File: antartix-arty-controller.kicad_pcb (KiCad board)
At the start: 2 copper layers, 68.5 x 40 mm, 77 parts, among them IC1 FT2232D, J1 QTE-020-04-L-D-A, J2 614004185023, J3 614004185023, J4 614004185023, J5 WE_629105150521, U1 PCT2075GVX, U2 PAC1934T-I_JQ, U3 USB2514B-I_M2, U4 TPS2051BDBVR, U5 TPS2051BDBVR, U6 TPS2051BDBVR, U7 TPS2051BDBVR, Y1 7C-24.000MBB-T, Y2 MQ-6.000-12-30_30_

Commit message: Layout update (WIP)
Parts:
- added C27: C_100n_0402, antartix-arty-controller-footprints:0402-cap, B.Cu at (160.1, 88.8)
- added D7: LG_L29K-G2J1-24-Z, antartix-arty-controller-footprints:LED_0603, F.Cu at (154.1, 61.0)
- added R28: R_0R_0805, antmicro-footprints:0805-res, B.Cu at (160.7, 84.8)
- added R29: R_0R_0805, antmicro-footprints:0805-res, B.Cu at (160.7, 87.2)
- added R30: R_47k_0402, antartix-arty-controller-footprints:0402-res, F.Cu at (152.8, 61.4)
- added R31: R_12k_0402, antmicro-footprints:0402-res, F.Cu at (153.5, 70.6)
- 3V0: renamed from 3V1; moved to F.Cu
- 5V0: renamed from 5V1; moved to F.Cu
- C10, C11, C12, C13, C14, C15, C16, C17, C18, C19, C20, C21, C23, C25, C9, D2, D3, D4, D5, FB1, R10, R11, R12, R13, R15, R16, R17, R19, R20, R21, R22, R25, R26, R27, U7: moved to F.Cu
- R23, R24, R4, R5, R6, R7, R8: moved to B.Cu
- moved R10 111.2 mm to (110.3, 80.3), turned to 0 degrees
- moved R12 109.5 mm to (110.3, 77.1), turned to 0 degrees
- moved R13 103.7 mm to (110.3, 75.4), turned to 0 degrees
- moved R11 98.9 mm to (110.3, 78.7)
- moved D5 88.8 mm to (113.1, 75.4), turned to 180 degrees
- moved D4 85.5 mm to (113.1, 77.1), turned to 180 degrees
- moved D3 85.5 mm to (113.1, 78.7), turned to 180 degrees
- moved D2 83.0 mm to (113.1, 80.3), turned to 180 degrees
- moved C26 76.5 mm to (136.9, 55.0), turned to 90 degrees
- moved 3V0 74.0 mm to (147.5, 59.1)
- moved 5V0 72.4 mm to (145.3, 59.1), turned to 270 degrees
- moved C24 70.9 mm to (135.2, 100.7), turned to 90 degrees
- moved R27 65.6 mm to (153.9, 82.7), turned to 0 degrees
- moved C22 65.4 mm to (138.2, 102.9), turned to 0 degrees
- moved C11 63.8 mm to (153.8, 78.1), turned to 180 degrees
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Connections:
- net /USB_D_N_CON renamed /USB_D_CON_N
- net /USB_D_N_FTDI renamed /USB_D_FTDI_N
- net /USB_D_P_CON renamed /USB_D_CON_P
- net /USB_D_P_FTDI renamed /USB_D_FTDI_P
- 3V0 pad 1: Net-(3V1-Pad1) -> VCC3V3
- D2 pad 1: VBUS1 -> VBUS1_S
- D3 pad 1: VBUS2 -> VBUS2_S
- D4 pad 1: VBUS3 -> VBUS3_S
- D5 pad 1: VBUS4 -> VBUS4_S
- J1 pad 1: Arty_USB_P -> VCC5V0
- J1 pad 10: GPIO20 -> GND
- J1 pad 11: GPIO13 -> GND
- J1 pad 12: GPIO16 -> /RESET_N
- J1 pad 13: GPIO06 -> Arty_USB_P
- J1 pad 14: GPIO12 -> /USB1_EN
- J1 pad 15: Net-(J1-Pad15) -> Arty_USB_N
- J1 pad 16: Net-(J1-Pad16) -> /USB2_EN
- J1 pad 17: Net-(J1-Pad17) -> GND
- J1 pad 18: Net-(J1-Pad18) -> /USB3_EN
- J1 pad 19: Net-(J1-Pad19) -> SCL0
- J1 pad 2: Net-(J1-Pad2) -> GND
- J1 pad 21: Net-(J1-Pad21) -> SDA0
- J1 pad 23: Net-(J1-Pad23) -> GND
- J1 pad 25: Net-(J1-Pad25) -> /~PWRDN
- J1 pad 27: VCC5V0 -> /SLOW_~ALERT
- J1 pad 28: GND -> Net-(J1-Pad28)
- J1 pad 29: VCC5V0 -> GND
- J1 pad 3: Arty_USB_N -> VCC5V0
- J1 pad 30: GND -> Net-(J1-Pad30)
- J1 pad 31: VCC5V0 -> /3V3_RPI
- J1 pad 32: GND -> Net-(J1-Pad32)
- J1 pad 33: VCC5V0 -> /3V3_RPI
- J1 pad 34: GND -> Net-(J1-Pad34)
- J1 pad 35: VCC5V0 -> GND
- J1 pad 36: GND -> Net-(J1-Pad36)
- J1 pad 37: SCL0 -> /3V3_SSD
- J1 pad 39: SDA0 -> /3V3_SSD
- J1 pad 4: Net-(J1-Pad4) -> GND
- J1 pad 5: Net-(J1-Pad5) -> VCC5V0
- J1 pad 6: Net-(J1-Pad6) -> GND
- J1 pad 7: GPIO26 -> VCC5V0
- J1 pad 8: GPIO21 -> GND
- J1 pad 9: GPIO19 -> VCC5V0
- R14 pad 1: Net-(R14-Pad1) -> VBUS4
- R14 pad 2: VBUS4 -> VBUS4_S
- R4 pad 1: VCC3V3 -> SCL0
- R4 pad 2: SCL0 -> VCC3V3
- R6 pad 1: Net-(R6-Pad1) -> VBUS2
- R6 pad 2: VBUS1 -> VBUS2_S
- R7 pad 1: Net-(R7-Pad1) -> VBUS1
- R7 pad 2: VBUS2 -> VBUS1_S
- R8 pad 1: Net-(R8-Pad1) -> VBUS3
- R8 pad 2: VBUS3 -> VBUS3_S
- U2 pad 10: Net-(R14-Pad1) -> VBUS4_S
- U2 pad 11: Net-(R6-Pad1) -> VBUS1_S
- U2 pad 13: Net-(R7-Pad1) -> VBUS2_S
- U2 pad 8: Net-(R8-Pad1) -> VBUS3_S
- U3 pad 28: Net-(U3-Pad28) -> /SUSP_IND
- U4 pad 1: VBUS1 -> VBUS1_S
- U5 pad 1: VBUS2 -> VBUS2_S
- U6 pad 1: VBUS3 -> VBUS3_S
- U7 pad 1: VBUS4 -> VBUS4_S
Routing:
- net Arty_USB_N: track 0.00 -> 22.0 mm, vias 0 -> 1
- net Arty_USB_P: track 0.00 -> 21.2 mm, vias 0 -> 1
- net /USB3_EN: track 0.00 -> 18.9 mm
- net /USB2_EN: track 0.00 -> 17.7 mm
- net VCC3V3: track 0.00 -> 17.4 mm
- net /USB1_EN: track 0.00 -> 16.4 mm
- net /USB_D_FTDI_N: track 0.00 -> 15.5 mm, vias 0 -> 1
- net /RESET_N: track 0.00 -> 15.4 mm
- net /USB_D_FTDI_P: track 0.00 -> 15.0 mm, vias 0 -> 1
- net Net-(C19-Pad1): track 0.00 -> 11.8 mm
- net /USB_D_CON_N: track 0.00 -> 10.7 mm, vias 0 -> 1
- net /USB_D_CON_P: track 0.00 -> 9.72 mm, vias 0 -> 1
- net Net-(C21-Pad1): track 0.00 -> 9.67 mm
- net VCC5V0: track 0.00 -> 7.43 mm
- net /3V3_SSD: track 0.00 -> 7.34 mm
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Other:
- net class Default: via_dia 0.8 -> 0.5; via_drill 0.4 -> 0.2
- net class USB added: clearance 0.15, trace_width 0.15, via_dia 0.5, via_drill 0.2
- rule trace_min: 0.2 -> 0.15
- rule via_min_drill: 0.3 -> 0.2
- rule via_min_size: 0.4 -> 0.3

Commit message: Component placement done
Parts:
- added C28: C_100n_0402, antartix-arty-controller-footprints:0402-cap, F.Cu at (122.0, 70.2)
- added C29: C_100n_0402, antartix-arty-controller-footprints:0402-cap, F.Cu at (122.0, 61.0)
- added C30: C_100n_0402, antartix-arty-controller-footprints:0402-cap, F.Cu at (161.3, 63.9)
- added C31: C_100n_0402, antartix-arty-controller-footprints:0402-cap, F.Cu at (122.0, 65.6)
- added C32: C_100n_0402, antartix-arty-controller-footprints:0402-cap, F.Cu at (115.2, 70.1)
- added C33: C_100n_0402, antartix-arty-controller-footprints:0402-cap, F.Cu at (166.4, 62.3)
- added C34: C_100n_0402, antartix-arty-controller-footprints:0402-cap, F.Cu at (115.1, 60.9)
- added C35: C_100n_0402, antartix-arty-controller-footprints:0402-cap, F.Cu at (115.2, 65.5)
- added C36: C_22u_0603, antmicro-footprints:0603-cap, F.Cu at (116.4, 70.1)
- added C37: C_22u_0603, antmicro-footprints:0603-cap, F.Cu at (165.2, 62.0)
- added C38: C_22u_0603, antmicro-footprints:0603-cap, F.Cu at (116.4, 61.0)
- added C39: C_22u_0603, antmicro-footprints:0603-cap, F.Cu at (116.4, 65.5)
- added R32: R_4k7_0402, antartix-arty-controller-footprints:0402-res, F.Cu at (151.8, 61.4)
- added R33: R_4k7_0402, antartix-arty-controller-footprints:0402-res, F.Cu at (145.1, 63.7)
- added R34: R_4k7_0402, antartix-arty-controller-footprints:0402-res, F.Cu at (145.1, 64.8)
- added R35: R_4k7_0402, antartix-arty-controller-footprints:0402-res, F.Cu at (149.2, 61.5)
- R23, R24: moved to F.Cu
- moved C24 21.1 mm to (139.3, 80.0), turned to 270 degrees
- moved R23 16.8 mm to (168.5, 78.1)
- moved R24 15.0 mm to (168.5, 77.1)
- moved C26 11.3 mm to (139.3, 66.0), turned to 270 degrees
- moved C22 9.03 mm to (139.3, 94.0), turned to 270 degrees
- moved C21 6.13 mm to (165.9, 79.6), turned to 90 degrees
- moved C10 3.81 mm to (150.3, 80.6)
- moved C15 3.81 mm to (150.3, 81.6)
- moved C20 3.81 mm to (163.6, 80.1)
- moved R15 3.81 mm to (158.9, 76.0)
- moved R17 3.81 mm to (163.6, 81.1)
- moved R18 3.81 mm to (157.6, 74.1)
- moved R19 3.81 mm to (150.4, 85.2)
- moved R20 3.81 mm to (150.4, 83.2)
- moved R22 3.81 mm to (155.0, 89.5)
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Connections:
- J1 pad 13: Arty_USB_P -> RP_USB_P
- J1 pad 15: Arty_USB_N -> RP_USB_N
- R23 pad 1: /USB_D_FTDI_N -> RP_USB_N
- R24 pad 1: /USB_D_FTDI_P -> RP_USB_P
- U3 pad 30: Arty_USB_N -> RP_USB_N
- U3 pad 31: Arty_USB_P -> RP_USB_P
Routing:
- net RP_USB_N: track 0.00 -> 25.2 mm, vias 0 -> 2
- net RP_USB_P: track 0.00 -> 24.4 mm, vias 0 -> 2
- net Arty_USB_N: track 22.0 -> 0.00 mm, vias 1 -> 0
- net Arty_USB_P: track 21.2 -> 0.00 mm, vias 1 -> 0
- net /USB_D_CON_P: track 9.72 -> 27.2 mm, vias 1 -> 0
- net /USB_D_CON_N: track 10.7 -> 27.2 mm, vias 1 -> 0
- net /USB_D_FTDI_N: track 15.5 -> 1.99 mm, vias 1 -> 0
- net /USB_D_FTDI_P: track 15.0 -> 1.99 mm, vias 1 -> 0
- net Net-(C19-Pad1): track 11.8 -> 14.2 mm
- net /OC_N1: track 0.00 -> 1.85 mm
- net /OC_N2: track 0.00 -> 1.67 mm
- net Net-(C21-Pad1): track 9.67 -> 10.8 mm
- net VCC3V3: track 17.4 -> 18.3 mm

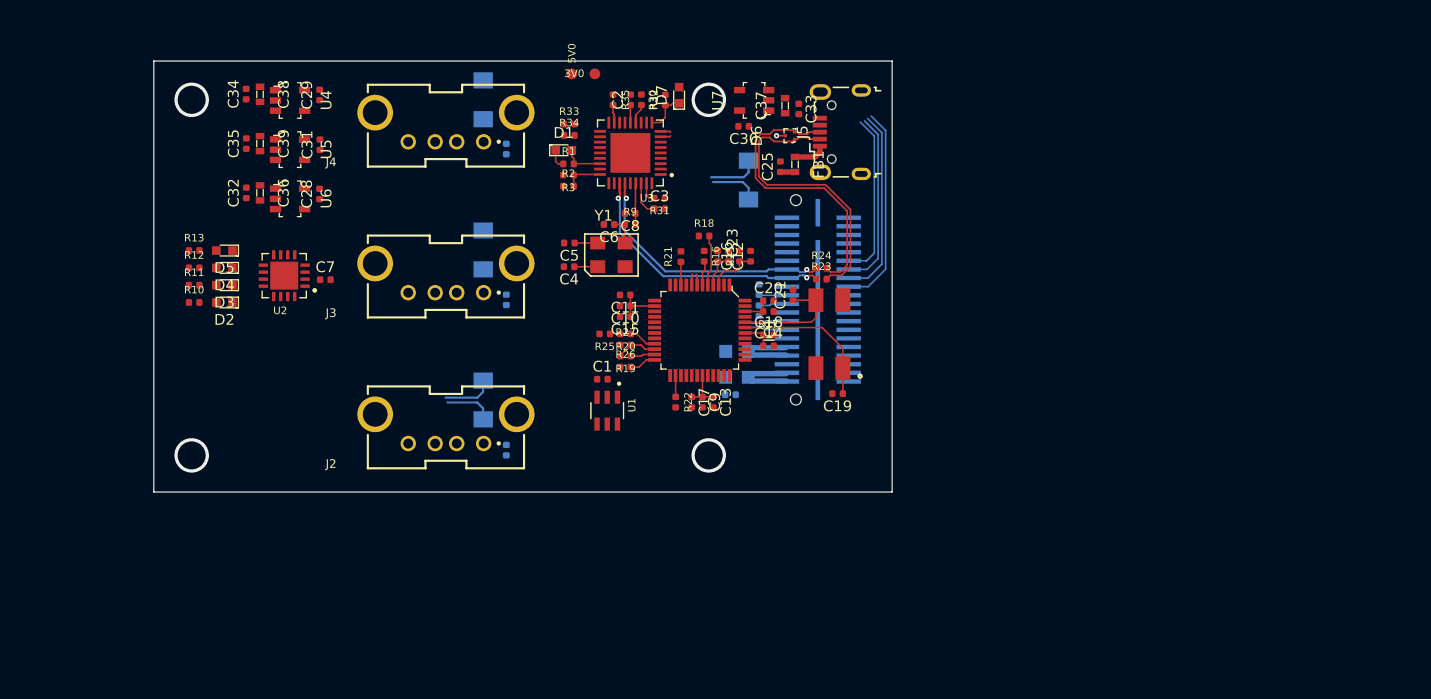
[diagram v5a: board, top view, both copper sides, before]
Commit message: Modified layout, routed USB. Now routing current sensing
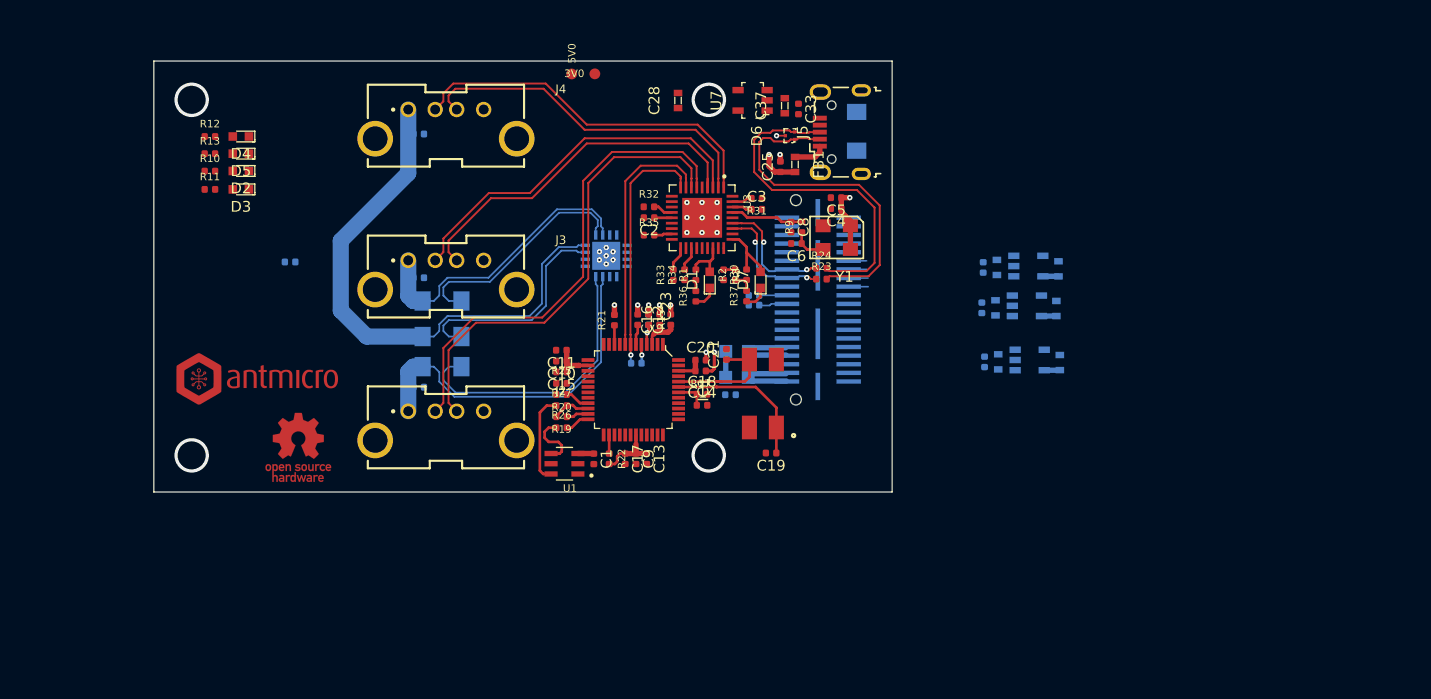
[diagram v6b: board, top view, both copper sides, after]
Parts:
- added N1: antmicro_logo, antmicro-footprints:antmicro-logo_scaled_15mm, F.Cu at (116.6, 87.4)
- added N2: oshw_logo, antmicro-footprints:oshw-logo, F.Cu at (120.0, 93.7)
- added R36: R_220R_0402, antartix-arty-controller-footprints:0402-res, F.Cu at (156.9, 79.7)
- added R37: R_220R_0402, antartix-arty-controller-footprints:0402-res, F.Cu at (161.6, 79.7)
- C28: value C_100n_0402 -> C_100n_0603; footprint antartix-arty-controller-footprints:0402-cap -> antmicro-footprints:0603-cap
- C29, C30, C31: value C_100n_0402 -> C_100n_0603; footprint antartix-arty-controller-footprints:0402-cap -> antmicro-footprints:0603-cap; moved to B.Cu
- C32, C34, C35, C36, C38, C39, C7, R16, R18, U2, U4, U5, U6: moved to B.Cu
- moved C31 71.6 mm to (190.7, 85.8)
- moved C34 71.1 mm to (183.4, 80.8), turned to 270 degrees
- moved C38 71.1 mm to (184.7, 80.8), turned to 90 degrees
- moved U4 71.0 mm to (187.6, 80.6), turned to 90 degrees
- moved C29 70.4 mm to (190.5, 77.1)
- moved C32 70.3 mm to (183.7, 85.8), turned to 270 degrees
- moved C36 70.3 mm to (184.9, 85.8), turned to 90 degrees
- moved U6 70.3 mm to (187.9, 85.6), turned to 90 degrees
- moved U5 69.4 mm to (187.7, 76.9), turned to 90 degrees
- moved C39 69.3 mm to (184.8, 77.0), turned to 90 degrees
- moved C35 69.3 mm to (183.6, 77.0), turned to 270 degrees
- moved C28 34.4 mm to (155.2, 61.5)
- moved C30 33.6 mm to (190.3, 80.8), turned to 90 degrees
- moved U2 29.9 mm to (148.6, 75.9)
- moved C4 25.4 mm to (169.9, 71.6)
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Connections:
- C22 pad 1: VBUS1 -> VBUS3
- C26 pad 1: VBUS3 -> VBUS1
- C28 pad 1: GND -> VCC5V0
- C28 pad 2: VCC5V0 -> GND
- C29 pad 1: GND -> VCC5V0
- C29 pad 2: VCC5V0 -> GND
- C30 pad 1: GND -> VCC5V0
- C30 pad 2: VCC5V0 -> GND
- C31 pad 1: GND -> VCC5V0
- C31 pad 2: VCC5V0 -> GND
- D1 pad 1: VCC3V3 -> Net-(D1-Pad1)
- D7 pad 1: VCC3V3 -> Net-(D7-Pad1)
- J2 pad 1: VBUS1 -> VBUS3
- J2 pad 2: /USB1_D_N -> /USB3_D_N
- J2 pad 3: /USB1_D_P -> /USB3_D_P
- J4 pad 1: VBUS3 -> VBUS1
- J4 pad 2: /USB3_D_P -> /USB1_D_N
- J4 pad 3: /USB3_D_N -> /USB1_D_P
- U3 pad 15: Net-(U3-Pad15) -> VCC3V3
- U3 pad 23: Net-(U3-Pad15) -> VCC3V3
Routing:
- net VBUS1: track 4.57 -> 50.8 mm
- net /USB3_D_N: track 0.00 -> 45.0 mm
- net /USB3_D_P: track 0.00 -> 43.4 mm
- net /USB2_D_N: track 0.00 -> 35.8 mm
- net /USB2_D_P: track 0.00 -> 34.3 mm
- net /USB1_D_N: track 0.00 -> 34.2 mm
- net VBUS3: track 0.00 -> 32.8 mm
- net /USB1_D_P: track 0.00 -> 32.6 mm
- net VBUS2: track 0.00 -> 27.4 mm
- net VBUS3_S: track 0.00 -> 26.5 mm
- net VBUS2_S: track 0.00 -> 21.6 mm
- net /USB_D_FTDI_P: track 1.99 -> 23.1 mm, vias 0 -> 1
- net /USB_D_FTDI_N: track 1.99 -> 22.9 mm
- net /USB3_EN: track 18.9 -> 1.81 mm
- net VBUS1_S: track 4.76 -> 20.7 mm
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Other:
- net class Default: clearance 0.2 -> 0.127
- net class USB removed
- rule trace_clearance: 0.2 -> 0.127

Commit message: Problem with power switches
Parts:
- C22, C24, C26, C7, R14, R6, R7, R8, U2: moved to F.Cu
- moved N1 52.9 mm to (169.5, 88.9), turned to 90 degrees
- moved 5V0 36.7 mm to (178.8, 73.9)
- moved 3V0 36.7 mm to (181.0, 74.0)
- moved U2 27.4 mm to (121.1, 75.4)
- moved C28 21.5 mm to (176.8, 62.3)
- moved C33 17.9 mm to (184.2, 63.2)
- moved C37 17.9 mm to (183.0, 62.9)
- moved U7 17.9 mm to (180.0, 62.4)
- moved R7 17.8 mm to (122.8, 69.1), turned to 180 degrees
- moved D3 17.6 mm to (98.4, 76.5)
- moved D5 17.6 mm to (98.4, 73.2)
- moved R11 17.6 mm to (95.5, 76.5)
- moved R13 17.6 mm to (95.5, 73.2)
- moved D2 17.6 mm to (98.4, 74.8)
- moved D4 17.6 mm to (98.4, 71.6)
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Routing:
- net VBUS1: track 50.8 -> 26.2 mm, vias 0 -> 2
- net VBUS2_S: track 21.6 -> 8.04 mm
- net VBUS2: track 27.4 -> 19.6 mm
- net VBUS4: track 3.72 -> 10.6 mm, vias 1 -> 2
- net VBUS1_S: track 20.7 -> 14.2 mm, vias 0 -> 2
- net VBUS3_S: track 26.5 -> 22.9 mm, vias 0 -> 2
- net VBUS4_S: track 0.00 -> 2.87 mm
- net VBUS3: track 32.8 -> 31.5 mm, vias 0 -> 2

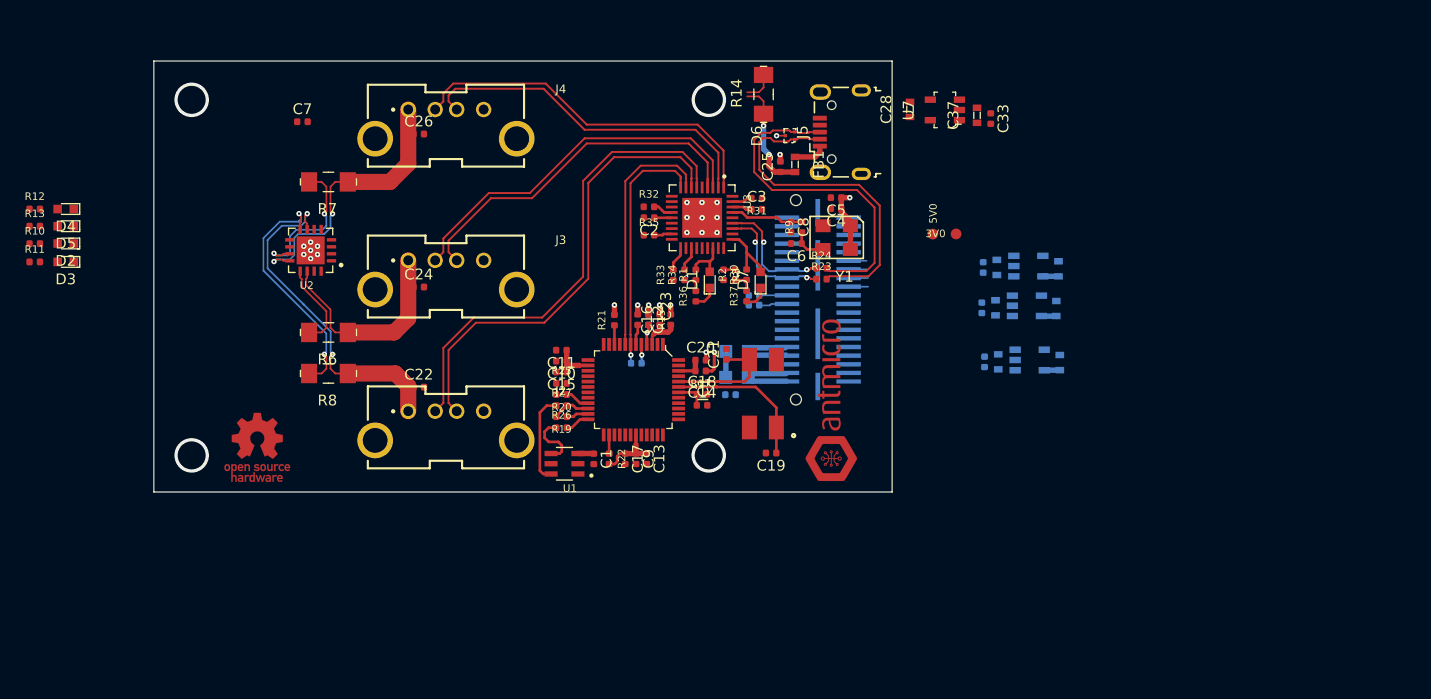
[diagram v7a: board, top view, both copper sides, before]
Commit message: Replace power switches
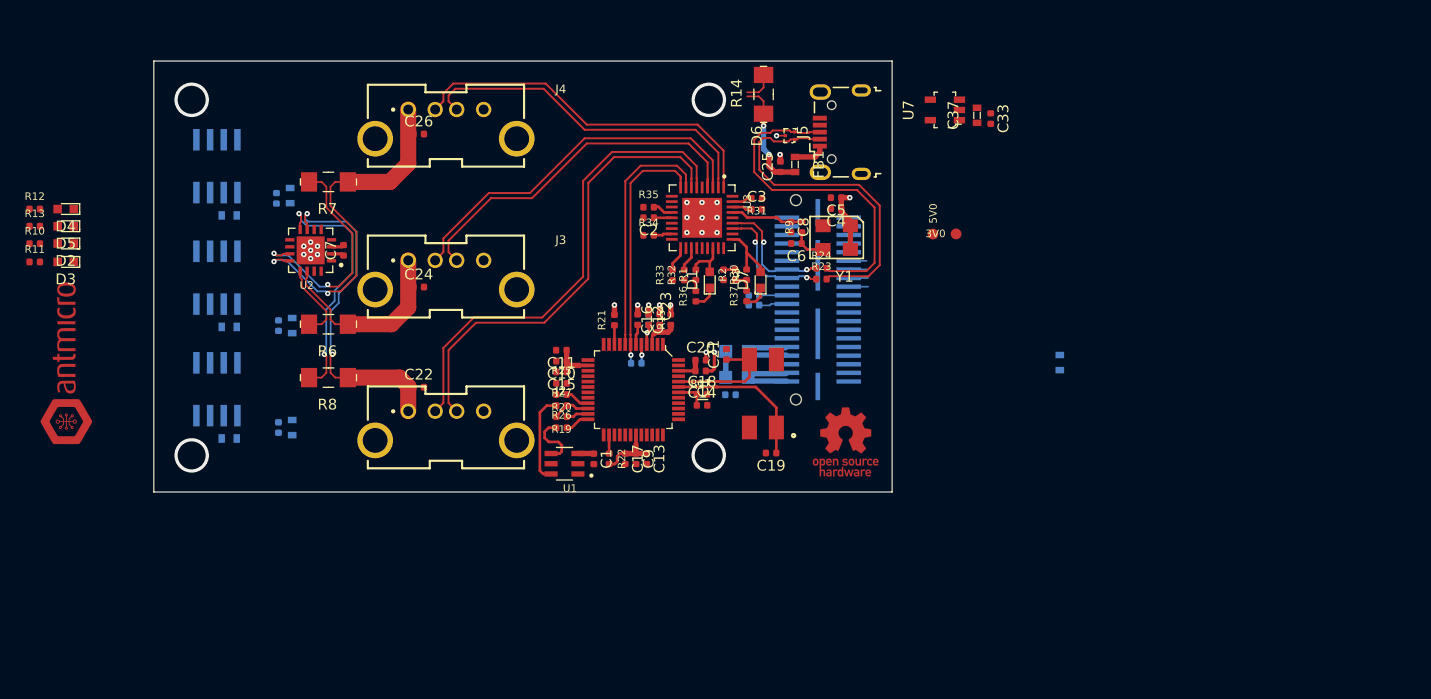
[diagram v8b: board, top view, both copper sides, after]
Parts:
- C28: moved to B.Cu
- U4, U5, U6: value TPS2051BDBVR -> TPS2024DR; footprint antartix-arty-controller-footprints:SOT-753 -> antartix-arty-controller-footprints:SOIC-8_W3.9mm
- moved C30 77.7 mm to (113.6, 92.9), turned to 0 degrees
- moved C29 77.2 mm to (113.6, 82.5), turned to 0 degrees
- moved U4 76.3 mm to (112.4, 67.6), turned to 180 degrees
- moved U6 75.5 mm to (112.4, 88.3), turned to 180 degrees
- moved U5 75.3 mm to (112.4, 78.0), turned to 180 degrees
- moved N1 71.1 mm to (98.5, 85.5)
- moved C35 67.1 mm to (118.1, 91.9), turned to 90 degrees
- moved C39 67.1 mm to (119.4, 91.9)
- moved C38 66.3 mm to (119.2, 70.3)
- moved C34 66.3 mm to (118.0, 70.6), turned to 90 degrees
- moved C32 65.6 mm to (118.1, 82.4), turned to 90 degrees
- moved C36 65.6 mm to (119.4, 82.4)
- moved C28 63.9 mm to (113.6, 72.2), turned to 0 degrees
- moved N2 54.6 mm to (170.8, 93.2)
- moved C7 12.5 mm to (124.2, 75.4), turned to 90 degrees
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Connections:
- C32 pad 2: VBUS3_S -> VBUS2_S
- C35 pad 2: VBUS2_S -> VBUS3_S
- C36 pad 1: VBUS3_S -> GND
- C36 pad 2: GND -> VBUS2_S
- C38 pad 1: VBUS1_S -> GND
- C38 pad 2: GND -> VBUS1_S
- C39 pad 1: VBUS2_S -> GND
- C39 pad 2: GND -> VBUS3_S
- R32 pad 2: /OC_N1 -> /OC_N4
- R34 pad 2: /OC_N4 -> /OC_N2
- R35 pad 2: /OC_N2 -> /OC_N1
- U2 pad 15: Net-(U2-Pad15) -> VCC5V0
- U4 pad 1: VBUS1_S -> GND
- U4 pad 2: GND -> VCC5V0
- U4 pad 3: /OC_N1 -> VCC5V0
- U4 pad 5: VCC5V0 -> /OC_N1
- U5 pad 1: VBUS2_S -> GND
- U5 pad 2: GND -> VCC5V0
- U5 pad 3: /OC_N2 -> VCC5V0
- U5 pad 5: VCC5V0 -> /OC_N2
- U6 pad 1: VBUS3_S -> GND
- U6 pad 2: GND -> VCC5V0
- U6 pad 3: /OC_N3 -> VCC5V0
- U6 pad 5: VCC5V0 -> /OC_N3
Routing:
- net VBUS1: track 26.2 -> 33.7 mm
- net VBUS1_S: track 14.2 -> 21.6 mm, vias 2 -> 3
- net VCC5V0: track 15.6 -> 12.5 mm
- net VBUS2: track 19.6 -> 17.9 mm
- net GND: track 4.84 -> 6.01 mm
- net VBUS2_S: track 8.04 -> 7.28 mm
- net VBUS3_S: track 22.9 -> 23.4 mm
- net Net-(SP3-Pad1): vias 1 -> 0
